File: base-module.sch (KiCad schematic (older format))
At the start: 0 parts

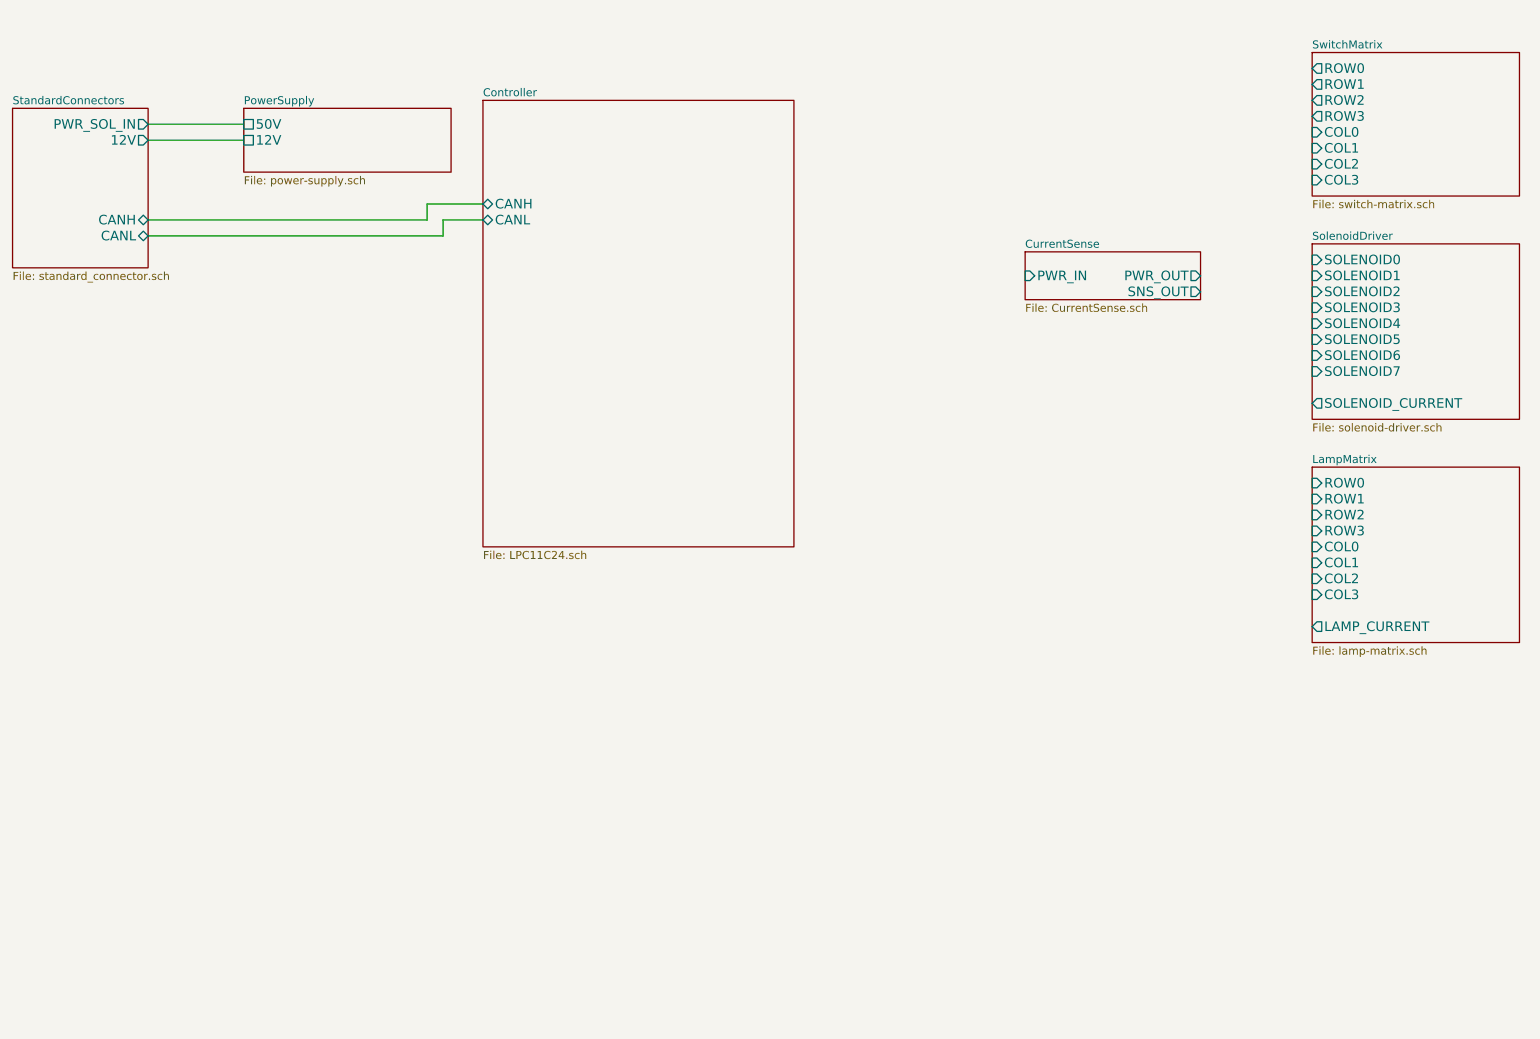
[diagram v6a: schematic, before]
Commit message: added the other two current sense outputs and modified the power circut, i cant seem to add the 9th pad, the bottom thermal pad????
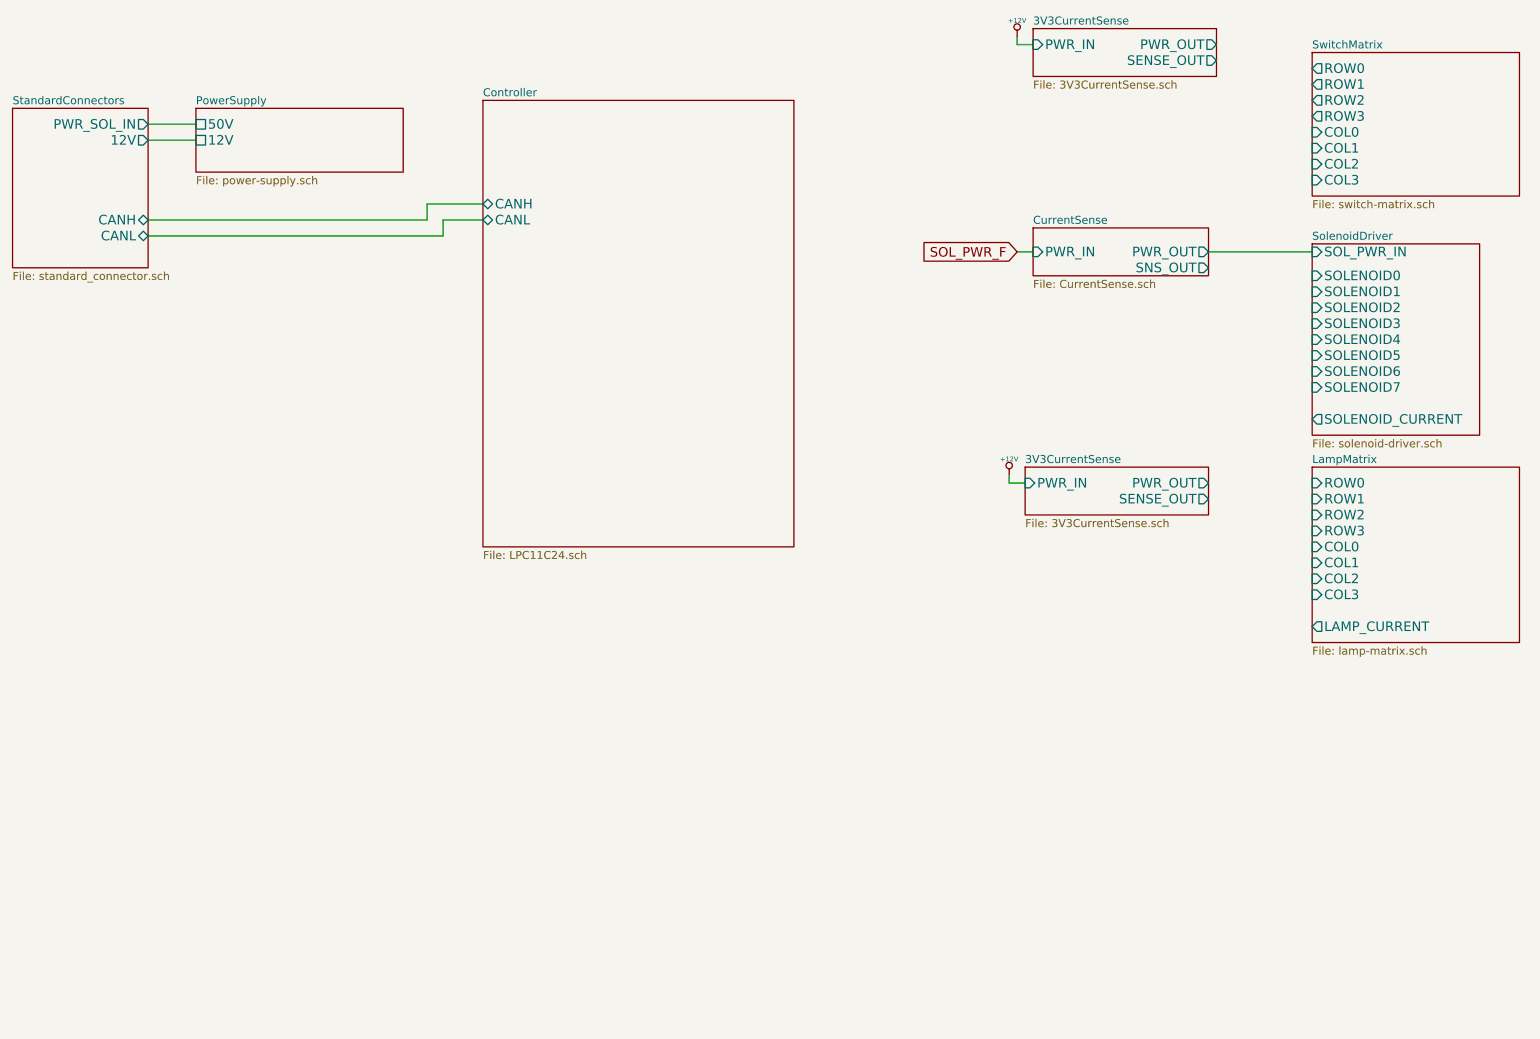
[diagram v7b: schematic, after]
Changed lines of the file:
@@
-EESchema Schematic File Version 2  date 4/16/2013 12:48:50 AM
+EESchema Schematic File Version 2  date 4/16/2013 2:34:18 AM
 LIBS:power
 LIBS:device
@@
 $Descr USLetter 11000 8500
 encoding utf-8
-Sheet 1 8
+Sheet 1 10
 Title ""
 Date "16 apr 2013"
@@
 $EndSheet
 $Sheet
-S 8750 2300 1300 1100
+S 8750 2300 1050 1200
 U 51638EDE
 F0 "SolenoidDriver" 50
 F1 "solenoid-driver.sch" 50
-F2 "SOLENOID0" I L 8750 2400 60
-F3 "SOLENOID1" I L 8750 2500 60
-F4 "SOLENOID2" I L 8750 2600 60
-F5 "SOLENOID3" I L 8750 2700 60
-F6 "SOLENOID4" I L 8750 2800 60
-F7 "SOLENOID5" I L 8750 2900 60
-F8 "SOLENOID6" I L 8750 3000 60
-F9 "SOLENOID7" I L 8750 3100 60
-F10 "SOLENOID_CURRENT" O L 8750 3300 60
+F2 "SOLENOID0" I L 8750 2500 60
+F3 "SOLENOID1" I L 8750 2600 60
+F4 "SOLENOID2" I L 8750 2700 60
+F5 "SOLENOID3" I L 8750 2800 60
+F6 "SOLENOID4" I L 8750 2900 60
+F7 "SOLENOID5" I L 8750 3000 60
+F8 "SOLENOID6" I L 8750 3100 60
+F9 "SOLENOID7" I L 8750 3200 60
+F10 "SOLENOID_CURRENT" O L 8750 3400 60
+F11 "SOL_PWR_IN" I L 8750 2350 60
 $EndSheet
 $Sheet
@@
 $EndSheet
 Wire Wire Line
-	1450 1650 2050 1650
-Wire Wire Line
-	1450 1550 2050 1550
-$Sheet
-S 2050 1450 1300 400
+	1450 1650 1750 1650
+Wire Wire Line
+	1450 1550 1750 1550
+$Sheet
+S 1750 1450 1300 400
 U 51638FEE
 F0 "PowerSupply" 50
 F1 "power-supply.sch" 50
-F2 "50V" U L 2050 1550 60
-F3 "12V" U L 2050 1650 60
+F2 "50V" U L 1750 1550 60
+F3 "12V" U L 1750 1650 60
 $EndSheet
 Wire Wire Line
@@
 	3300 2250 1450 2250
 $Sheet
-S 6950 2350 1100 300
+S 7000 2200 1100 300
 U 516CAB4E
 F0 "CurrentSense" 50
 F1 "CurrentSense.sch" 50
-F2 "PWR_IN" I L 6950 2500 60
-F3 "PWR_OUT" O R 8050 2500 60
-F4 "SNS_OUT" O R 8050 2600 60
+F2 "PWR_IN" I L 7000 2350 60
+F3 "PWR_OUT" O R 8100 2350 60
+F4 "SNS_OUT" O R 8100 2450 60
 $EndSheet
 $Sheet
@@
 F5 "12V" O R 1450 1650 60
 $EndSheet
+Wire Wire Line
+	8100 2350 8750 2350
+Text GLabel 6900 2350 0    60   Input ~ 0
+SOL_PWR_F
+Wire Wire Line
+	7000 2350 6900 2350
+$Sheet
+S 7000 950  1150 300
+U 516D5B3C
+F0 "3V3CurrentSense" 50
+F1 "3V3CurrentSense.sch" 50
+F2 "PWR_IN" I L 7000 1050 60
+F3 "PWR_OUT" O R 8150 1050 60
+F4 "SENSE_OUT" O R 8150 1150 60
+$EndSheet
+$Sheet
+S 6950 3700 1150 300
+U 516D6DB7
+F0 "3V3CurrentSense" 50
+F1 "3V3CurrentSense.sch" 50
+F2 "PWR_IN" I L 6950 3800 60
+F3 "PWR_OUT" O R 8100 3800 60
+F4 "SENSE_OUT" O R 8100 3900 60
+$EndSheet
+$Comp
+L +12V #PWR?
+U 1 1 516D8357
+P 6850 3750
+F 0 "#PWR?" H 6850 3700 20  0001 C CNN
+F 1 "+12V" H 6850 3850 30  0000 C CNN
+F 2 "" H 6850 3750 60  0000 C CNN
+F 3 "" H 6850 3750 60  0000 C CNN
+	1    6850 3750
+	1    0    0    -1
+$EndComp
+$Comp
+L +12V #PWR?
+U 1 1 516D85FA
+P 6900 1000
+F 0 "#PWR?" H 6900 950 20  0001 C CNN
+F 1 "+12V" H 6900 1100 30  0000 C CNN
+F 2 "" H 6900 1000 60  0000 C CNN
+F 3 "" H 6900 1000 60  0000 C CNN
+	1    6900 1000
+	1    0    0    -1
+$EndComp
+Wire Wire Line
+	6900 1000 6900 1050
+Wire Wire Line
+	6900 1050 7000 1050
+Wire Wire Line
+	6850 3750 6850 3800
+Wire Wire Line
+	6850 3800 6950 3800
 $EndSCHEMATC

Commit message: added dip switch library and modifed current sense's to add capsstarted the main controller page
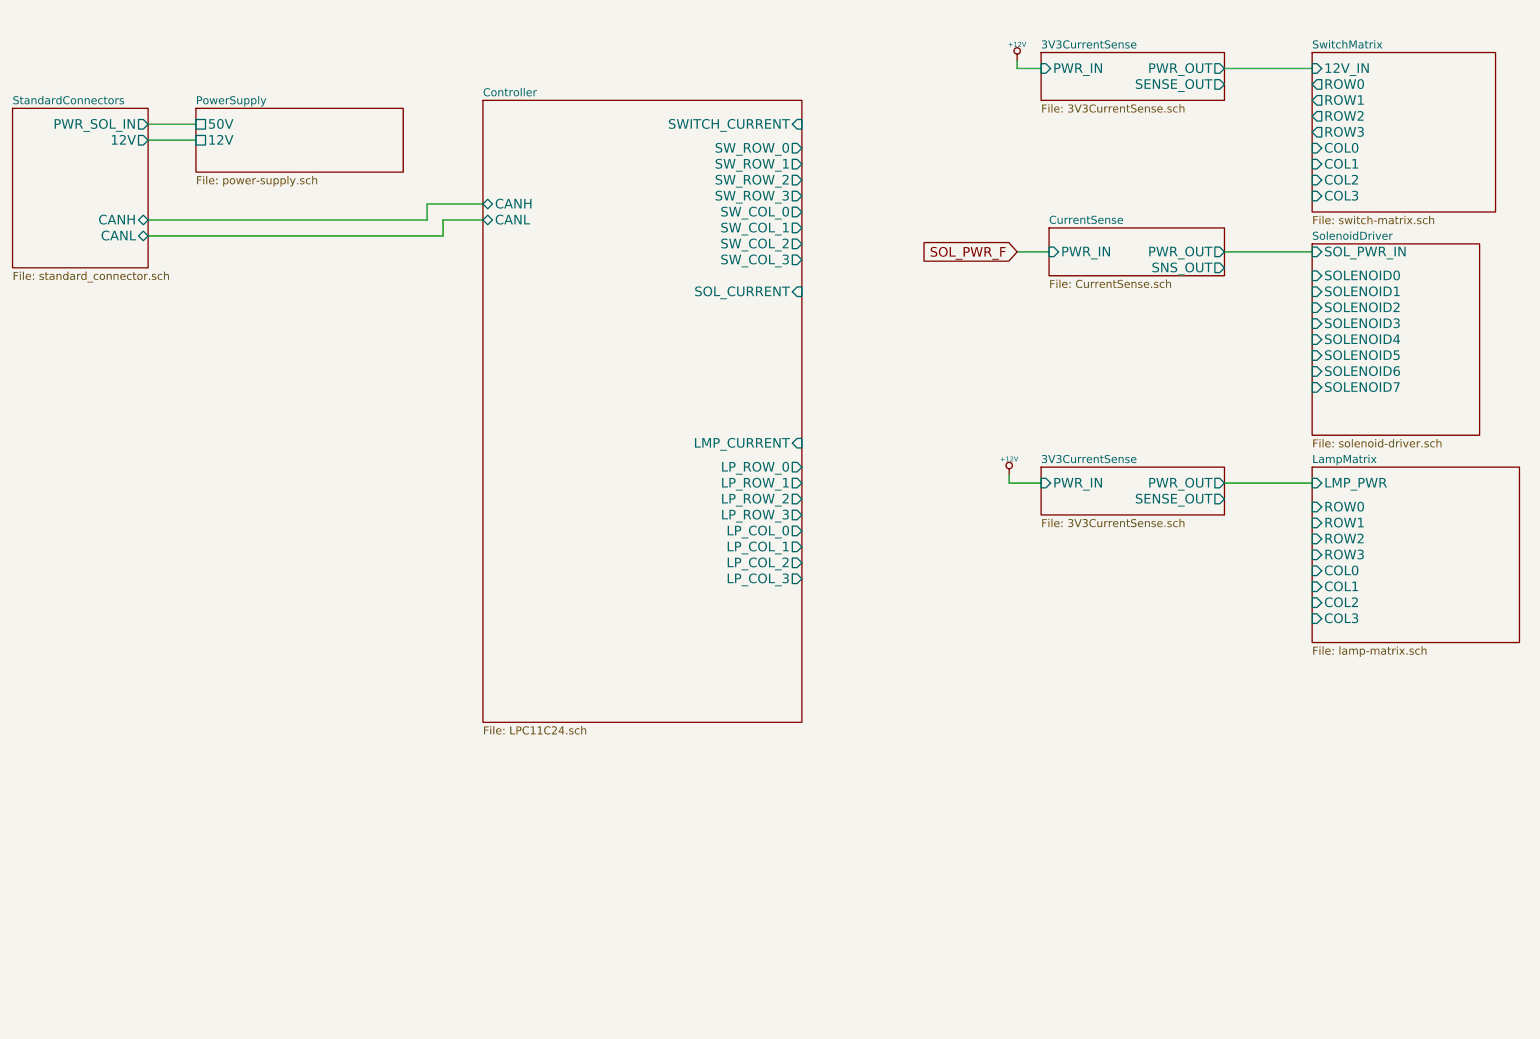
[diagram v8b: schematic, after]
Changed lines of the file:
@@
-EESchema Schematic File Version 2  date 4/16/2013 2:34:18 AM
+EESchema Schematic File Version 2  date 4/16/2013 9:07:53 PM
 LIBS:power
 LIBS:device
@@
 LIBS:CurrentSense
 LIBS:pinball-power
+LIBS:dips-s
 LIBS:base-module-cache
 EELAYER 27 0
@@
 Sheet 1 10
 Title ""
-Date "16 apr 2013"
+Date "17 apr 2013"
 Rev ""
 Comp ""
@@
 $EndDescr
 $Sheet
-S 8750 1100 1300 900
+S 8750 1100 1150 1000
 U 51638E9B
 F0 "SwitchMatrix" 50
 F1 "switch-matrix.sch" 50
-F2 "ROW0" O L 8750 1200 60
-F3 "ROW1" O L 8750 1300 60
-F4 "ROW2" O L 8750 1400 60
-F5 "ROW3" O L 8750 1500 60
-F6 "COL0" I L 8750 1600 60
-F7 "COL1" I L 8750 1700 60
-F8 "COL2" I L 8750 1800 60
-F9 "COL3" I L 8750 1900 60
+F2 "ROW0" O L 8750 1300 60
+F3 "ROW1" O L 8750 1400 60
+F4 "ROW2" O L 8750 1500 60
+F5 "ROW3" O L 8750 1600 60
+F6 "COL0" I L 8750 1700 60
+F7 "COL1" I L 8750 1800 60
+F8 "COL2" I L 8750 1900 60
+F9 "COL3" I L 8750 2000 60
+F10 "12V_IN" I L 8750 1200 60
 $EndSheet
 $Sheet
@@
 F0 "LampMatrix" 50
 F1 "lamp-matrix.sch" 50
-F2 "ROW0" I L 8750 3800 60
-F3 "ROW1" I L 8750 3900 60
-F4 "ROW2" I L 8750 4000 60
-F5 "ROW3" I L 8750 4100 60
-F6 "COL0" I L 8750 4200 60
-F7 "COL1" I L 8750 4300 60
-F8 "COL2" I L 8750 4400 60
-F9 "COL3" I L 8750 4500 60
-F10 "LAMP_CURRENT" O L 8750 4700 60
+F2 "ROW0" I L 8750 3950 60
+F3 "ROW1" I L 8750 4050 60
+F4 "ROW2" I L 8750 4150 60
+F5 "ROW3" I L 8750 4250 60
+F6 "COL0" I L 8750 4350 60
+F7 "COL1" I L 8750 4450 60
+F8 "COL2" I L 8750 4550 60
+F9 "COL3" I L 8750 4650 60
+F10 "LMP_PWR" I L 8750 3800 60
 $EndSheet
 $Sheet
@@
 F8 "SOLENOID6" I L 8750 3100 60
 F9 "SOLENOID7" I L 8750 3200 60
-F10 "SOLENOID_CURRENT" O L 8750 3400 60
-F11 "SOL_PWR_IN" I L 8750 2350 60
-$EndSheet
-$Sheet
-S 3550 1400 1950 2800
-U 516A58DE
-F0 "Controller" 50
-F1 "LPC11C24.sch" 50
-F2 "CANH" B L 3550 2050 60
-F3 "CANL" B L 3550 2150 60
+F10 "SOL_PWR_IN" I L 8750 2350 60
 $EndSheet
 Wire Wire Line
@@
 	3300 2250 1450 2250
 $Sheet
-S 7000 2200 1100 300
+S 7100 2200 1100 300
 U 516CAB4E
 F0 "CurrentSense" 50
 F1 "CurrentSense.sch" 50
-F2 "PWR_IN" I L 7000 2350 60
-F3 "PWR_OUT" O R 8100 2350 60
-F4 "SNS_OUT" O R 8100 2450 60
+F2 "PWR_IN" I L 7100 2350 60
+F3 "PWR_OUT" O R 8200 2350 60
+F4 "SNS_OUT" O R 8200 2450 60
 $EndSheet
 $Sheet
@@
 $EndSheet
 Wire Wire Line
-	8100 2350 8750 2350
+	8200 2350 8750 2350
 Text GLabel 6900 2350 0    60   Input ~ 0
 SOL_PWR_F
 Wire Wire Line
-	7000 2350 6900 2350
-$Sheet
-S 7000 950  1150 300
+	7100 2350 6900 2350
+$Sheet
+S 7050 1100 1150 300
 U 516D5B3C
 F0 "3V3CurrentSense" 50
 F1 "3V3CurrentSense.sch" 50
-F2 "PWR_IN" I L 7000 1050 60
-F3 "PWR_OUT" O R 8150 1050 60
-F4 "SENSE_OUT" O R 8150 1150 60
-$EndSheet
-$Sheet
-S 6950 3700 1150 300
+F2 "PWR_IN" I L 7050 1200 60
+F3 "PWR_OUT" O R 8200 1200 60
+F4 "SENSE_OUT" O R 8200 1300 60
+$EndSheet
+$Sheet
+S 7050 3700 1150 300
 U 516D6DB7
 F0 "3V3CurrentSense" 50
 F1 "3V3CurrentSense.sch" 50
-F2 "PWR_IN" I L 6950 3800 60
-F3 "PWR_OUT" O R 8100 3800 60
-F4 "SENSE_OUT" O R 8100 3900 60
+F2 "PWR_IN" I L 7050 3800 60
+F3 "PWR_OUT" O R 8200 3800 60
+F4 "SENSE_OUT" O R 8200 3900 60
 $EndSheet
 $Comp
@@
 L +12V #PWR?
 U 1 1 516D85FA
-P 6900 1000
-F 0 "#PWR?" H 6900 950 20  0001 C CNN
-F 1 "+12V" H 6900 1100 30  0000 C CNN
-F 2 "" H 6900 1000 60  0000 C CNN
-F 3 "" H 6900 1000 60  0000 C CNN
-	1    6900 1000
+P 6900 1150
+F 0 "#PWR?" H 6900 1100 20  0001 C CNN
+F 1 "+12V" H 6900 1250 30  0000 C CNN
+F 2 "" H 6900 1150 60  0000 C CNN
+F 3 "" H 6900 1150 60  0000 C CNN
+	1    6900 1150
 	1    0    0    -1
 $EndComp
 Wire Wire Line
-	6900 1000 6900 1050
-Wire Wire Line
-	6900 1050 7000 1050
+	6900 1150 6900 1200
+Wire Wire Line
+	6900 1200 7050 1200
 Wire Wire Line
 	6850 3750 6850 3800
 Wire Wire Line
-	6850 3800 6950 3800
+	6850 3800 7050 3800
+Wire Wire Line
+	8200 1200 8750 1200
+Wire Wire Line
+	8200 3800 8750 3800
+$Sheet
+S 3550 1400 2000 3900
+U 516A58DE
+F0 "Controller" 50
+F1 "LPC11C24.sch" 50
+F2 "CANH" B L 3550 2050 60
+F3 "CANL" B L 3550 2150 60
+F4 "LP_ROW_0" O R 5550 3700 60
+F5 "LP_ROW_1" O R 5550 3800 60
+F6 "LP_ROW_2" O R 5550 3900 60
+F7 "LP_ROW_3" O R 5550 4000 60
+F8 "LP_COL_0" O R 5550 4100 60
+F9 "LP_COL_1" O R 5550 4200 60
+F10 "LP_COL_2" O R 5550 4300 60
+F11 "LP_COL_3" O R 5550 4400 60
+F12 "SOL_CURRENT" I R 5550 2600 60
+F13 "SW_ROW_0" O R 5550 1700 60
+F14 "SW_ROW_1" O R 5550 1800 60
+F15 "SW_ROW_2" O R 5550 1900 60
+F16 "SW_ROW_3" O R 5550 2000 60
+F17 "SW_COL_0" O R 5550 2100 60
+F18 "SW_COL_1" O R 5550 2200 60
+F19 "SW_COL_2" O R 5550 2300 60
+F20 "SW_COL_3" O R 5550 2400 60
+F21 "LMP_CURRENT" I R 5550 3550 60
+F22 "SWITCH_CURRENT" I R 5550 1550 60
+$EndSheet
 $EndSCHEMATC
